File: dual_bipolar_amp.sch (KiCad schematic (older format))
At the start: 9 parts, among them U4 OPA2156xD

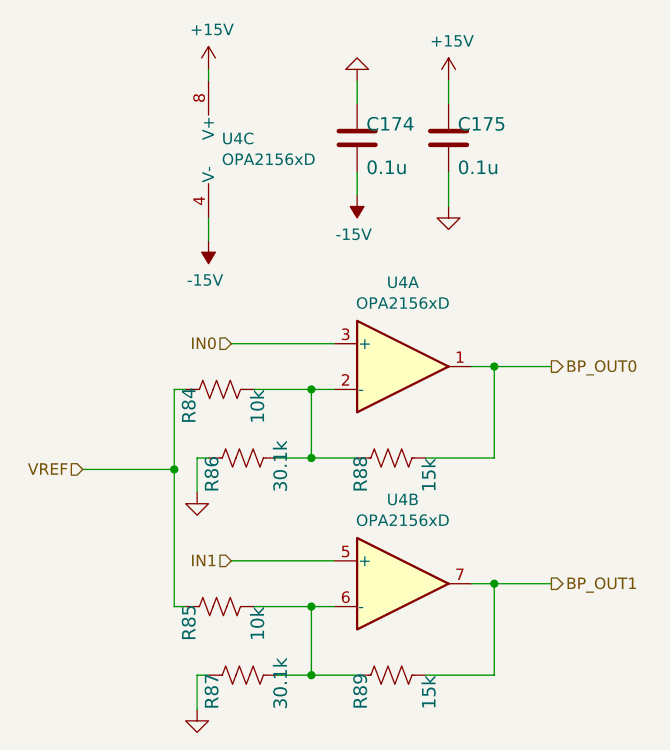
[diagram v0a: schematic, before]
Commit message: updates after bug in ADS8686 power connectivity. And swap of DC SCL and SDA
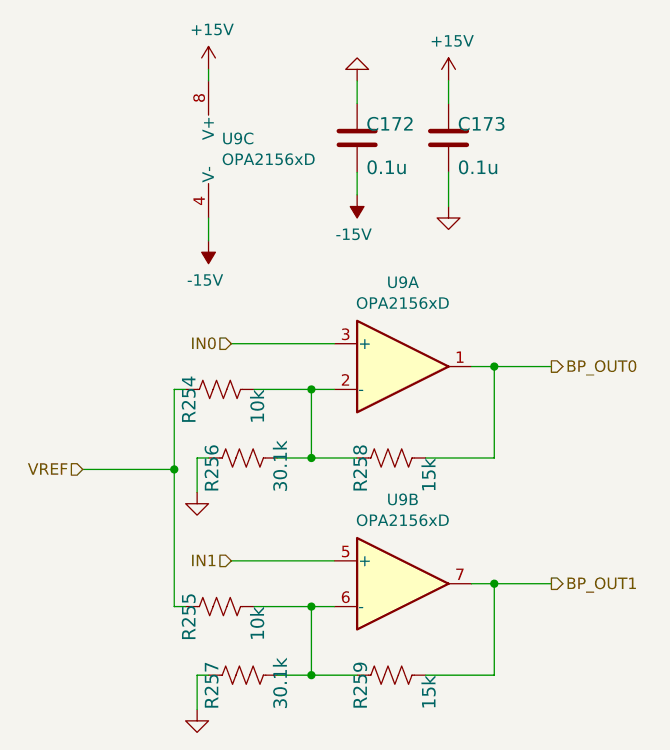
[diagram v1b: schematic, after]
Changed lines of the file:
@@
 AR Path="/6095BD4C/60EB6FD5/60F31C8B" Ref="U2"  Part="1"
 AR Path="/61B02572/60EB6FD5/60F31C8B" Ref="U9"  Part="1"
-F 0 "U4" H 5600 3617 50  0000 C CNN
+F 0 "U9" H 5600 3617 50  0000 C CNN
 F 1 "OPA2156xD" H 5600 3526 50  0000 C CNN
 F 2 "Package_SO:SOIC-8_3.9x4.9mm_P1.27mm" H 5700 3250 50  0001 C CNN
@@
 AR Path="/6095BD4C/60EB6FD5/60F31C94" Ref="R3"  Part="1"
 AR Path="/61B02572/60EB6FD5/60F31C94" Ref="R254"  Part="1"
-F 0 "R84" H 4650 3450 59  0000 L BNN
+F 0 "R254" H 4650 3450 59  0000 L BNN
 F 1 "10k" H 4650 3150 59  0000 L BNN
 F 2 "Resistor_SMD:R_0603_1608Metric" H 4800 3350 50  0001 C CNN
@@
 AR Path="/6095BD4C/60EB6FD5/60F31C9B" Ref="U2"  Part="3"
 AR Path="/61B02572/60EB6FD5/60F31C9B" Ref="U9"  Part="3"
-F 0 "U4" H 4808 2346 50  0000 L CNN
+F 0 "U9" H 4808 2346 50  0000 L CNN
 F 1 "OPA2156xD" H 4808 2255 50  0000 L CNN
 F 2 "Package_SO:SOIC-8_3.9x4.9mm_P1.27mm" H 4850 2300 50  0001 C CNN
@@
 AR Path="/6095BD4C/60EB6FD5/60F31CA4" Ref="R7"  Part="1"
 AR Path="/61B02572/60EB6FD5/60F31CA4" Ref="R256"  Part="1"
-F 0 "R86" H 4750 3750 59  0000 L BNN
+F 0 "R256" H 4750 3750 59  0000 L BNN
 F 1 "30.1k" H 4750 3450 59  0000 L BNN
 F 2 "Resistor_SMD:R_0603_1608Metric" H 4900 3650 50  0001 C CNN
@@
 AR Path="/6095BD4C/60EB6FD5/60F31CB1" Ref="R13"  Part="1"
 AR Path="/61B02572/60EB6FD5/60F31CB1" Ref="R258"  Part="1"
-F 0 "R88" H 5400 3750 59  0000 L BNN
+F 0 "R258" H 5400 3750 59  0000 L BNN
 F 1 "15k" H 5400 3450 59  0000 L BNN
 F 2 "Resistor_SMD:R_0603_1608Metric" H 5550 3650 50  0001 C CNN
@@
 AR Path="/6095BD4C/60EB6FD5/60F31CB8" Ref="U2"  Part="2"
 AR Path="/61B02572/60EB6FD5/60F31CB8" Ref="U9"  Part="2"
-F 0 "U4" H 5600 4567 50  0000 C CNN
+F 0 "U9" H 5600 4567 50  0000 C CNN
 F 1 "OPA2156xD" H 5600 4476 50  0000 C CNN
 F 2 "Package_SO:SOIC-8_3.9x4.9mm_P1.27mm" H 5700 4200 50  0001 C CNN
@@
 AR Path="/6095BD4C/60EB6FD5/60F31CC1" Ref="R4"  Part="1"
 AR Path="/61B02572/60EB6FD5/60F31CC1" Ref="R255"  Part="1"
-F 0 "R85" H 4650 4400 59  0000 L BNN
+F 0 "R255" H 4650 4400 59  0000 L BNN
 F 1 "10k" H 4650 4100 59  0000 L BNN
 F 2 "Resistor_SMD:R_0603_1608Metric" H 4800 4300 50  0001 C CNN
@@
 AR Path="/6095BD4C/60EB6FD5/60F31CCA" Ref="R8"  Part="1"
 AR Path="/61B02572/60EB6FD5/60F31CCA" Ref="R257"  Part="1"
-F 0 "R87" H 4750 4700 59  0000 L BNN
+F 0 "R257" H 4750 4700 59  0000 L BNN
 F 1 "30.1k" H 4750 4400 59  0000 L BNN
 F 2 "Resistor_SMD:R_0603_1608Metric" H 4900 4600 50  0001 C CNN
@@
 AR Path="/6095BD4C/60EB6FD5/60F31CD7" Ref="R14"  Part="1"
 AR Path="/61B02572/60EB6FD5/60F31CD7" Ref="R259"  Part="1"
-F 0 "R89" H 5400 4700 59  0000 L BNN
+F 0 "R259" H 5400 4700 59  0000 L BNN
 F 1 "15k" H 5400 4400 59  0000 L BNN
 F 2 "Resistor_SMD:R_0603_1608Metric" H 5550 4600 50  0001 C CNN
@@
 AR Path="/6095BD4C/60EB6FD5/60F31CED" Ref="C5"  Part="1"
 AR Path="/61B02572/60EB6FD5/60F31CED" Ref="C172"  Part="1"
-F 0 "C174" H 5440 2275 59  0000 L BNN
+F 0 "C172" H 5440 2275 59  0000 L BNN
 F 1 "0.1u" H 5440 2085 59  0000 L BNN
 F 2 "Capacitor_SMD:C_0603_1608Metric" H 5400 2250 50  0001 C CNN
@@
 AR Path="/6095BD4C/60EB6FD5/60F31CF7" Ref="C6"  Part="1"
 AR Path="/61B02572/60EB6FD5/60F31CF7" Ref="C173"  Part="1"
-F 0 "C175" H 5840 2275 59  0000 L BNN
+F 0 "C173" H 5840 2275 59  0000 L BNN
 F 1 "0.1u" H 5840 2085 59  0000 L BNN
 F 2 "Capacitor_SMD:C_0603_1608Metric" H 5800 2250 50  0001 C CNN

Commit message: before importing autoroute
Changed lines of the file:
@@
 $Descr A4 11693 8268
 encoding utf-8
-Sheet 26 26
+Sheet 23 26
 Title ""
 Date ""
@@
 AR Path="/6095BD4C/60EB6FD5/60F31C8B" Ref="U2"  Part="1"
 AR Path="/61B02572/60EB6FD5/60F31C8B" Ref="U9"  Part="1"
-F 0 "U9" H 5600 3617 50  0000 C CNN
+F 0 "U4" H 5600 3617 50  0000 C CNN
 F 1 "OPA2156xD" H 5600 3526 50  0000 C CNN
 F 2 "Package_SO:SOIC-8_3.9x4.9mm_P1.27mm" H 5700 3250 50  0001 C CNN
@@
 AR Path="/6095BD4C/60EB6FD5/60F31C94" Ref="R3"  Part="1"
 AR Path="/61B02572/60EB6FD5/60F31C94" Ref="R254"  Part="1"
-F 0 "R254" H 4650 3450 59  0000 L BNN
+F 0 "R84" H 4650 3450 59  0000 L BNN
 F 1 "10k" H 4650 3150 59  0000 L BNN
 F 2 "Resistor_SMD:R_0603_1608Metric" H 4800 3350 50  0001 C CNN
@@
 AR Path="/6095BD4C/60EB6FD5/60F31C9B" Ref="U2"  Part="3"
 AR Path="/61B02572/60EB6FD5/60F31C9B" Ref="U9"  Part="3"
-F 0 "U9" H 4808 2346 50  0000 L CNN
+F 0 "U4" H 4808 2346 50  0000 L CNN
 F 1 "OPA2156xD" H 4808 2255 50  0000 L CNN
 F 2 "Package_SO:SOIC-8_3.9x4.9mm_P1.27mm" H 4850 2300 50  0001 C CNN
@@
 AR Path="/6095BD4C/60EB6FD5/60F31CA4" Ref="R7"  Part="1"
 AR Path="/61B02572/60EB6FD5/60F31CA4" Ref="R256"  Part="1"
-F 0 "R256" H 4750 3750 59  0000 L BNN
+F 0 "R86" H 4750 3750 59  0000 L BNN
 F 1 "30.1k" H 4750 3450 59  0000 L BNN
 F 2 "Resistor_SMD:R_0603_1608Metric" H 4900 3650 50  0001 C CNN
@@
 AR Path="/6095BD4C/60EB6FD5/60F31CB1" Ref="R13"  Part="1"
 AR Path="/61B02572/60EB6FD5/60F31CB1" Ref="R258"  Part="1"
-F 0 "R258" H 5400 3750 59  0000 L BNN
+F 0 "R88" H 5400 3750 59  0000 L BNN
 F 1 "15k" H 5400 3450 59  0000 L BNN
 F 2 "Resistor_SMD:R_0603_1608Metric" H 5550 3650 50  0001 C CNN
@@
 AR Path="/6095BD4C/60EB6FD5/60F31CB8" Ref="U2"  Part="2"
 AR Path="/61B02572/60EB6FD5/60F31CB8" Ref="U9"  Part="2"
-F 0 "U9" H 5600 4567 50  0000 C CNN
+F 0 "U4" H 5600 4567 50  0000 C CNN
 F 1 "OPA2156xD" H 5600 4476 50  0000 C CNN
 F 2 "Package_SO:SOIC-8_3.9x4.9mm_P1.27mm" H 5700 4200 50  0001 C CNN
@@
 AR Path="/6095BD4C/60EB6FD5/60F31CC1" Ref="R4"  Part="1"
 AR Path="/61B02572/60EB6FD5/60F31CC1" Ref="R255"  Part="1"
-F 0 "R255" H 4650 4400 59  0000 L BNN
+F 0 "R85" H 4650 4400 59  0000 L BNN
 F 1 "10k" H 4650 4100 59  0000 L BNN
 F 2 "Resistor_SMD:R_0603_1608Metric" H 4800 4300 50  0001 C CNN
@@
 AR Path="/6095BD4C/60EB6FD5/60F31CCA" Ref="R8"  Part="1"
 AR Path="/61B02572/60EB6FD5/60F31CCA" Ref="R257"  Part="1"
-F 0 "R257" H 4750 4700 59  0000 L BNN
+F 0 "R87" H 4750 4700 59  0000 L BNN
 F 1 "30.1k" H 4750 4400 59  0000 L BNN
 F 2 "Resistor_SMD:R_0603_1608Metric" H 4900 4600 50  0001 C CNN
@@
 AR Path="/6095BD4C/60EB6FD5/60F31CD7" Ref="R14"  Part="1"
 AR Path="/61B02572/60EB6FD5/60F31CD7" Ref="R259"  Part="1"
-F 0 "R259" H 5400 4700 59  0000 L BNN
+F 0 "R89" H 5400 4700 59  0000 L BNN
 F 1 "15k" H 5400 4400 59  0000 L BNN
 F 2 "Resistor_SMD:R_0603_1608Metric" H 5550 4600 50  0001 C CNN
@@
 AR Path="/6095BD4C/60EB6FD5/60F31CED" Ref="C5"  Part="1"
 AR Path="/61B02572/60EB6FD5/60F31CED" Ref="C172"  Part="1"
-F 0 "C172" H 5440 2275 59  0000 L BNN
+F 0 "C174" H 5440 2275 59  0000 L BNN
 F 1 "0.1u" H 5440 2085 59  0000 L BNN
 F 2 "Capacitor_SMD:C_0603_1608Metric" H 5400 2250 50  0001 C CNN
@@
 AR Path="/6095BD4C/60EB6FD5/60F31CF7" Ref="C6"  Part="1"
 AR Path="/61B02572/60EB6FD5/60F31CF7" Ref="C173"  Part="1"
-F 0 "C173" H 5840 2275 59  0000 L BNN
+F 0 "C175" H 5840 2275 59  0000 L BNN
 F 1 "0.1u" H 5840 2085 59  0000 L BNN
 F 2 "Capacitor_SMD:C_0603_1608Metric" H 5800 2250 50  0001 C CNN
